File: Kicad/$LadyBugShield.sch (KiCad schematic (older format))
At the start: 8 parts, among them P1 CONN_6, P2 CONN_2, P3 BNC, P4 BNC

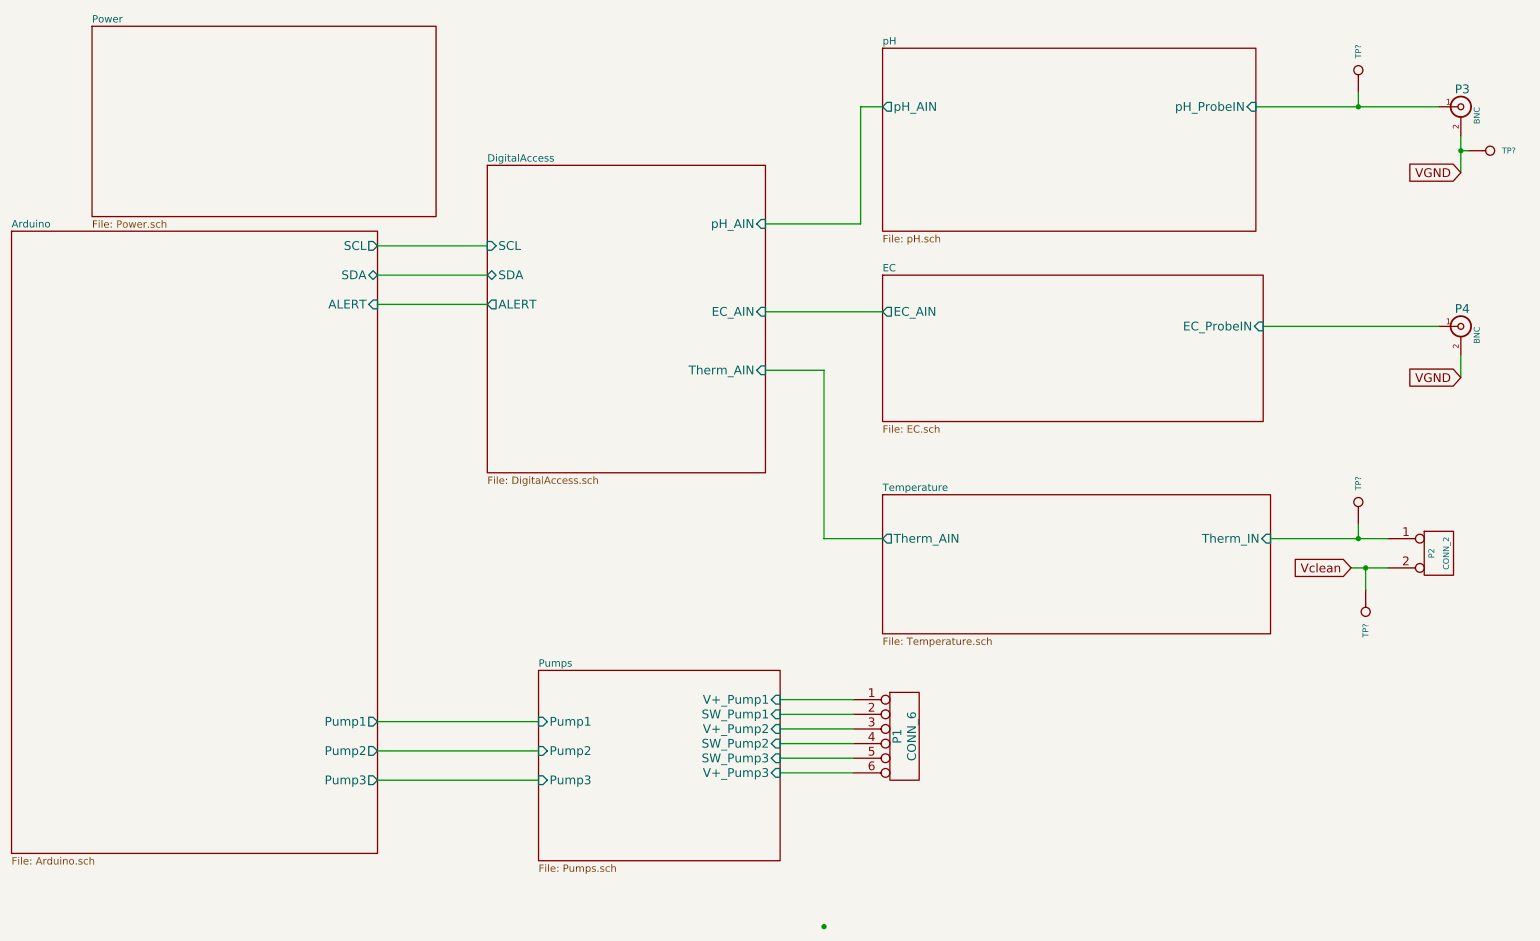
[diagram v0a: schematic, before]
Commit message: changed diodes added test points
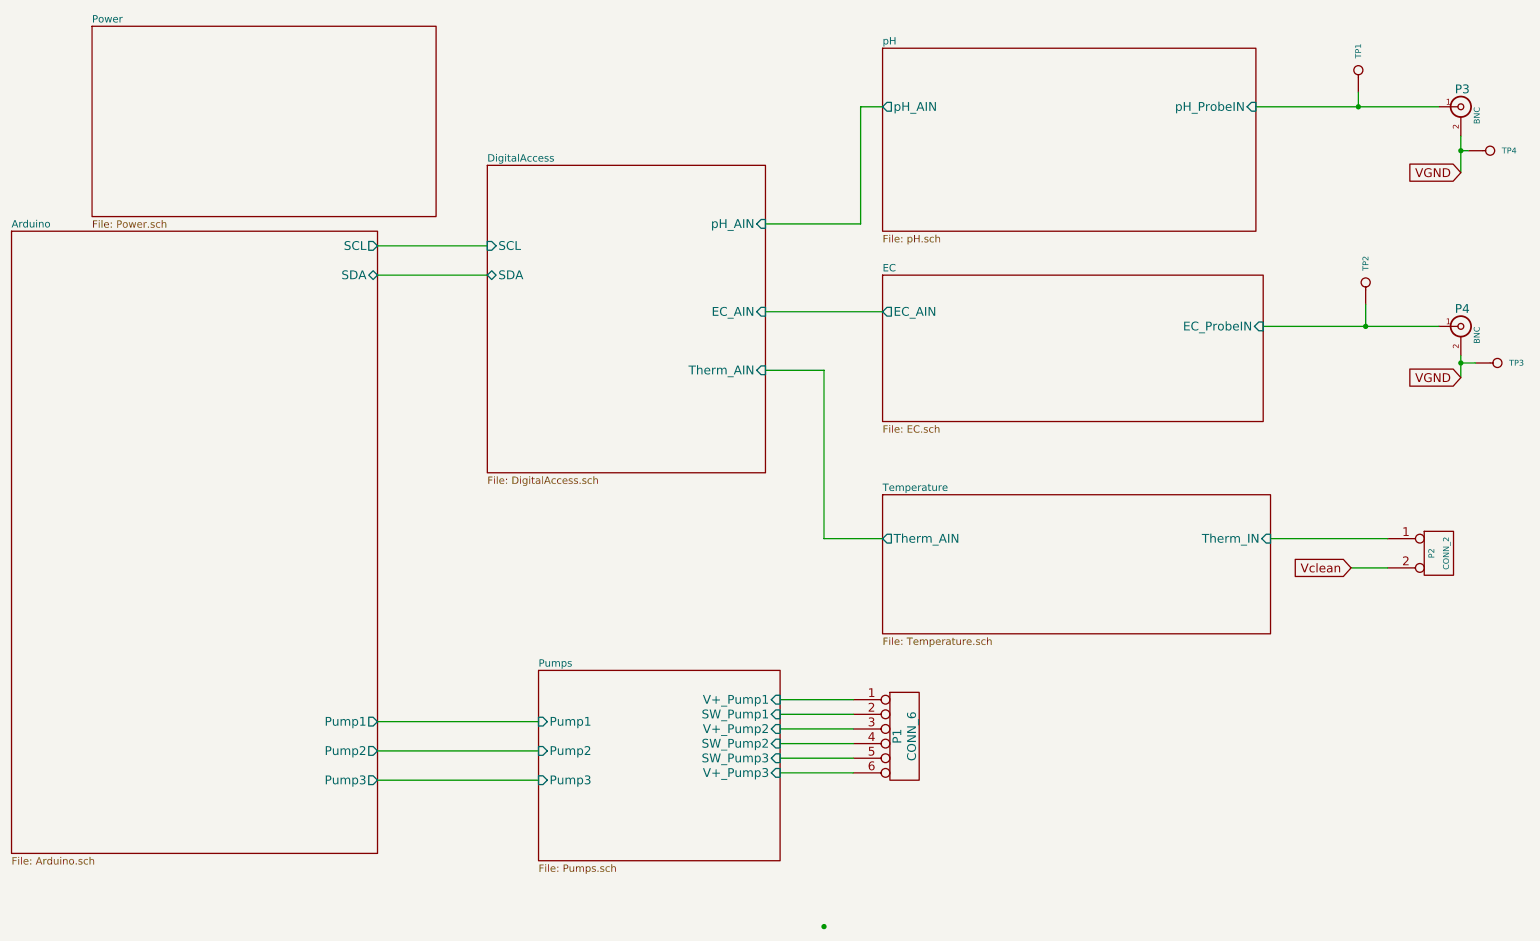
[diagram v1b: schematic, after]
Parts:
- gave numbers to parts that had none: 4
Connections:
- net EC/EC_ProbeIN: now also TP2.1
- net Temperature/Therm_IN: no longer TP2.1
- net VGND: now also TP3.1
- net Vclean: no longer TP3.1
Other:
- moved on the sheet: TP2, TP3
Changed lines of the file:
@@
 F5 "Pump1" O R 3300 5450 60
 F6 "Pump3" O R 3300 5850 60
-F7 "ALERT" I R 3300 2600 60
 $EndSheet
 $Sheet
@@
 F2 "SCL" I L 4050 2200 60
 F3 "SDA" B L 4050 2400 60
-F4 "ALERT" O L 4050 2600 60
-F5 "pH_AIN" I R 5950 2050 60
-F6 "EC_AIN" I R 5950 2650 60
-F7 "Therm_AIN" I R 5950 3050 60
+F4 "pH_AIN" I R 5950 2050 60
+F5 "EC_AIN" I R 5950 2650 60
+F6 "Therm_AIN" I R 5950 3050 60
 $EndSheet
 $Sheet
@@
 Wire Wire Line
 	3300 2400 4050 2400
-Wire Wire Line
-	3300 2600 4050 2600
 Connection ~ 6350 6850
 $Sheet
@@
 	6050 5800 6550 5800
 $Comp
-L CONN_1 TP?
+L CONN_1 TP1
 U 1 1 54956214
 P 10000 1000
-F 0 "TP?" H 10080 1000 40  0000 L CNN
+F 0 "TP1" H 10080 1000 40  0000 L CNN
 F 1 "CONN_1" H 10000 1055 30  0001 C CNN
 F 2 "" H 10000 1000 60  0000 C CNN
@@
 $EndComp
 $Comp
-L CONN_1 TP?
+L CONN_1 TP4
 U 1 1 54956279
 P 10900 1550
-F 0 "TP?" H 10980 1550 40  0000 L CNN
+F 0 "TP4" H 10980 1550 40  0000 L CNN
 F 1 "CONN_1" H 10900 1605 30  0001 C CNN
 F 2 "" H 10900 1550 60  0000 C CNN
@@
 $EndComp
 $Comp
-L CONN_1 TP?
+L CONN_1 TP2
 U 1 1 5495627F
-P 10000 3950
-F 0 "TP?" H 10080 3950 40  0000 L CNN
-F 1 "CONN_1" H 10000 4005 30  0001 C CNN
-F 2 "" H 10000 3950 60  0000 C CNN
-F 3 "" H 10000 3950 60  0000 C CNN
-	1    10000 3950
+P 10050 2450
+F 0 "TP2" H 10130 2450 40  0000 L CNN
+F 1 "CONN_1" H 10050 2505 30  0001 C CNN
+F 2 "" H 10050 2450 60  0000 C CNN
+F 3 "" H 10050 2450 60  0000 C CNN
+	1    10050 2450
 	0    -1   -1   0
 $EndComp
 $Comp
-L CONN_1 TP?
+L CONN_1 TP3
 U 1 1 54956285
-P 10050 4700
-F 0 "TP?" H 10130 4700 40  0000 L CNN
-F 1 "CONN_1" H 10050 4755 30  0001 C CNN
-F 2 "" H 10050 4700 60  0000 C CNN
-F 3 "" H 10050 4700 60  0000 C CNN
-	1    10050 4700
-	0    1    1    0
+P 10950 3000
+F 0 "TP3" H 11030 3000 40  0000 L CNN
+F 1 "CONN_1" H 10950 3055 30  0001 C CNN
+F 2 "" H 10950 3000 60  0000 C CNN
+F 3 "" H 10950 3000 60  0000 C CNN
+	1    10950 3000
+	1    0    0    -1
 $EndComp
 Wire Wire Line
@@
 Connection ~ 10700 1550
 Wire Wire Line
-	10000 4100 10000 4200
-Connection ~ 10000 4200
-Wire Wire Line
-	10050 4550 10050 4400
-Connection ~ 10050 4400
+	10050 2600 10050 2750
+Connection ~ 10050 2750
+Wire Wire Line
+	10800 3000 10700 3000
+Connection ~ 10700 3000
 $EndSCHEMATC
